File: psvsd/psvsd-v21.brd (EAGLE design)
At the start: 30 x 33.2 mm, 21 parts, among them U1 GL823(A)OG, U2 3.3V

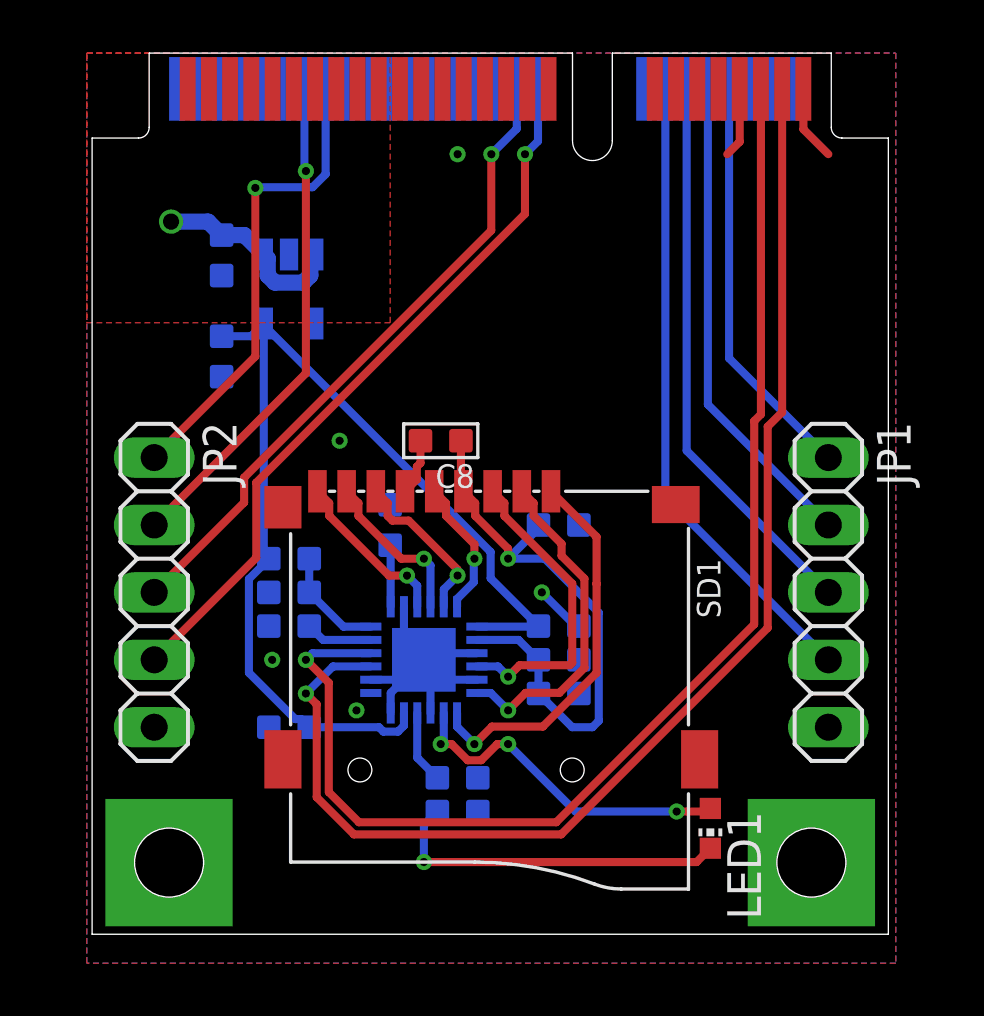
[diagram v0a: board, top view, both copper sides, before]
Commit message: Finished silkscreen and added BOM for v2.1 design
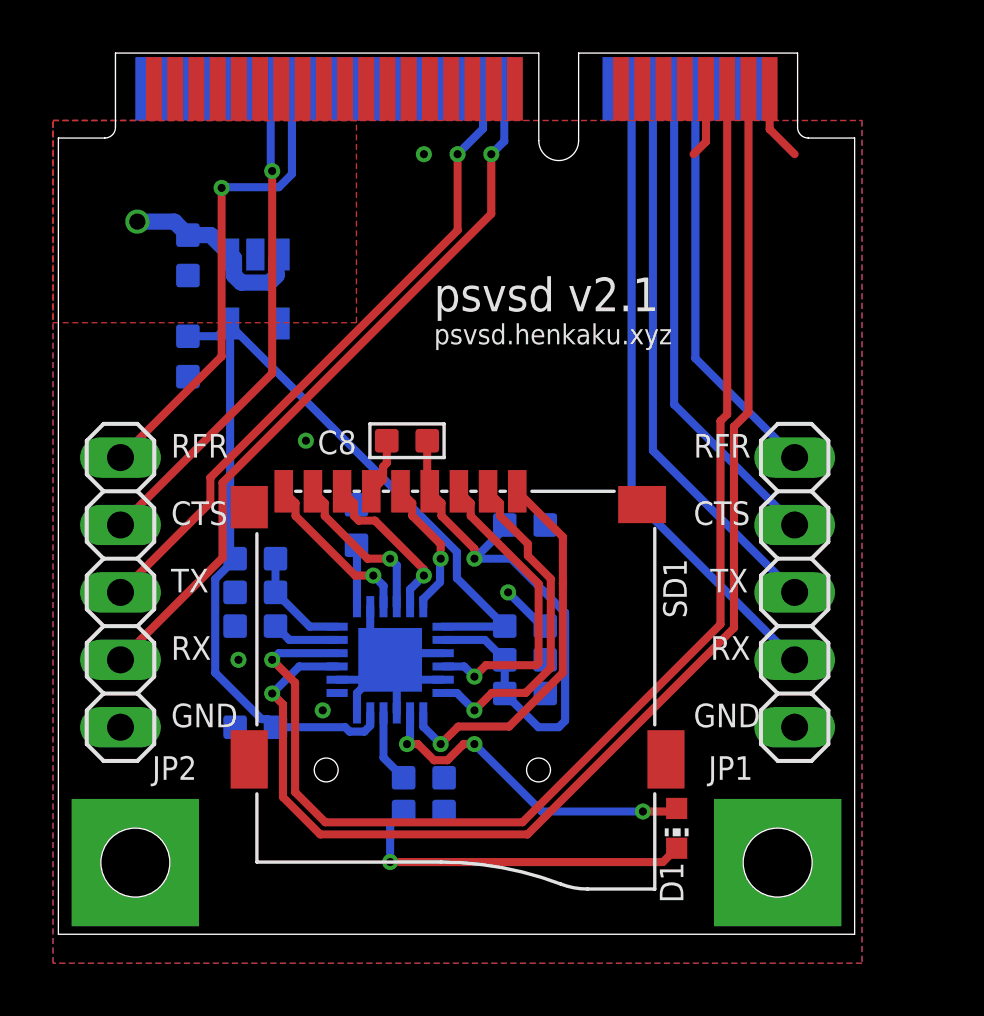
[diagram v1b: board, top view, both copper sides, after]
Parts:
- removed LED1: BLUE, led:CHIP-LED0603
- added D1: BLUE, led:CHIP-LED0603
- moved SD1 1.27 mm to (15.2, 17.8)
- moved U1 1.27 mm to (12.7, 11.4)
- moved C2 1.27 mm to (7.62, 14.0)
- moved C7 1.27 mm to (7.62, 8.89)
- moved FB1 1.27 mm to (7.62, 15.2)
- moved R1 1.27 mm to (7.62, 12.7)
- moved U2 1.27 mm to (7.62, 25.4)
- moved JP2 1.27 mm to (2.54, 14.0)
- moved C1 1.27 mm to (14.0, 6.99)
- moved C10 1.27 mm to (5.08, 26.7)
- moved C3 1.27 mm to (17.8, 11.4)
- moved C4 1.27 mm to (17.8, 16.5)
- moved C5 1.27 mm to (11.4, 16.5)
- moved C6 1.27 mm to (17.8, 12.7)
- moved C8 1.27 mm to (13.3, 19.7)
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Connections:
- net LED: now also D1.A; no longer LED1.A
- net LED_N: now also D1.C; no longer LED1.C
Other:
- outline, holes or cut-outs redrawn
- board text added: "CTS"
- board text added: "GND"
- board text added: "RFR"
- board text added: "RX"
- board text added: "TX"
- board text added: "psvsd v2.1"
- board text added: "psvsd.henkaku.xyz"

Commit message: Fixed problem where shield is not grounded
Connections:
- net GND: now also SD1.G1, SD1.G2, SD1.G3, SD1.G4
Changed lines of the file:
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@@
 <element name="C1" library="Seeed-Capacitor" library_urn="urn:adsk.eagle:library:464" package="C0603" value="0.1uF" x="13.97" y="6.985" smashed="yes" rot="MR270">
 <attribute name="MPN" value="GRM1885C1H102JA01D" x="13.97" y="6.985" size="1.778" layer="28" rot="MR270" display="off"/>
+<attribute name="NAME" x="12.7" y="7.239" size="0.635" layer="34" ratio="10" rot="MR180"/>
 <attribute name="NAME" x="17.145" y="6.604" size="0.889" layer="26" ratio="11" rot="MR0"/>
-<attribute name="NAME" x="12.7" y="7.239" size="0.635" layer="34" ratio="10" rot="MR180"/>
 <attribute name="VALUE" x="12.7" y="7.3025" size="0.635" layer="28" ratio="10" rot="MR180"/>
 </element>
 <element name="C10" library="Seeed-Capacitor" library_urn="urn:adsk.eagle:library:464" package="C0603" value="1uF" x="5.08" y="26.67" smashed="yes" rot="MR0">
 <attribute name="MPN" value="GRM1885C1H102JA01D" x="5.08" y="26.67" size="1.778" layer="28" rot="MR0" display="off"/>
+<attribute name="NAME" x="5.461" y="31.115" size="0.889" layer="26" ratio="11" rot="MR270"/>
 <attribute name="NAME" x="5.334" y="27.94" size="0.635" layer="34" ratio="10" rot="MR270"/>
-<attribute name="NAME" x="5.461" y="31.115" size="0.889" layer="26" ratio="11" rot="MR270"/>
 <attribute name="VALUE" x="5.3975" y="27.94" size="0.635" layer="28" ratio="10" rot="MR270"/>
 </element>
 <element name="C2" library="Seeed-Capacitor" library_urn="urn:adsk.eagle:library:464" package="C0603" value="0.1uF" x="7.62" y="13.97" smashed="yes" rot="MR90">
 <attribute name="MPN" value="GRM1885C1H102JA01D" x="7.62" y="13.97" size="1.778" layer="28" rot="MR90" display="off"/>
+<attribute name="NAME" x="8.89" y="13.716" size="0.635" layer="34" ratio="10" rot="MR0"/>
 <attribute name="NAME" x="5.715" y="13.589" size="0.889" layer="26" ratio="11" rot="MR0"/>
-<attribute name="NAME" x="8.89" y="13.716" size="0.635" layer="34" ratio="10" rot="MR0"/>
 <attribute name="VALUE" x="8.89" y="13.6525" size="0.635" layer="28" ratio="10" rot="MR0"/>
 </element>
 <element name="C3" library="Seeed-Capacitor" library_urn="urn:adsk.eagle:library:464" package="C0603" value="0.1uF" x="17.78" y="11.43" smashed="yes" rot="MR270">
 <attribute name="MPN" value="GRM1885C1H102JA01D" x="17.78" y="11.43" size="1.778" layer="28" rot="MR270" display="off"/>
+<attribute name="NAME" x="16.51" y="11.684" size="0.635" layer="34" ratio="10" rot="MR180"/>
 <attribute name="NAME" x="19.685" y="11.811" size="0.889" layer="26" ratio="11" rot="MR180"/>
-<attribute name="NAME" x="16.51" y="11.684" size="0.635" layer="34" ratio="10" rot="MR180"/>
 <attribute name="VALUE" x="16.51" y="11.7475" size="0.635" layer="28" ratio="10" rot="MR180"/>
 </element>
 <element name="C4" library="Seeed-Capacitor" library_urn="urn:adsk.eagle:library:464" package="C0603" value="10uF" x="17.78" y="16.51" smashed="yes" rot="MR270">
 <attribute name="MPN" value="GRM1885C1H102JA01D" x="17.78" y="16.51" size="1.778" layer="28" rot="MR270" display="off"/>
+<attribute name="NAME" x="16.51" y="16.764" size="0.635" layer="34" ratio="10" rot="MR180"/>
 <attribute name="NAME" x="19.685" y="16.891" size="0.889" layer="26" ratio="11" rot="MR180"/>
-<attribute name="NAME" x="16.51" y="16.764" size="0.635" layer="34" ratio="10" rot="MR180"/>
 <attribute name="VALUE" x="16.51" y="18.0975" size="0.635" layer="28" ratio="10" rot="MR180"/>
 </element>
 <element name="C5" library="Seeed-Capacitor" library_urn="urn:adsk.eagle:library:464" package="C0603" value="0.1uF" x="11.43" y="16.51" smashed="yes" rot="MR180">
 <attribute name="MPN" value="GRM1885C1H102JA01D" x="11.43" y="16.51" size="1.778" layer="28" rot="MR180" display="off"/>
+<attribute name="NAME" x="11.176" y="15.24" size="0.635" layer="34" ratio="10" rot="MR90"/>
 <attribute name="NAME" x="11.049" y="18.415" size="0.889" layer="26" ratio="11" rot="MR90"/>
-<attribute name="NAME" x="11.176" y="15.24" size="0.635" layer="34" ratio="10" rot="MR90"/>
 <attribute name="VALUE" x="11.1125" y="15.24" size="0.635" layer="28" ratio="10" rot="MR90"/>
 </element>
 <element name="C6" library="Seeed-Capacitor" library_urn="urn:adsk.eagle:library:464" package="C0603" value="0.1uF" x="17.78" y="12.7" smashed="yes" rot="MR270">
 <attribute name="MPN" value="GRM1885C1H102JA01D" x="17.78" y="12.7" size="1.778" layer="28" rot="MR270" display="off"/>
+<attribute name="NAME" x="16.51" y="12.954" size="0.635" layer="34" ratio="10" rot="MR180"/>
 <attribute name="NAME" x="19.685" y="13.081" size="0.889" layer="26" ratio="11" rot="MR180"/>
-<attribute name="NAME" x="16.51" y="12.954" size="0.635" layer="34" ratio="10" rot="MR180"/>
 <attribute name="VALUE" x="16.51" y="13.0175" size="0.635" layer="28" ratio="10" rot="MR180"/>
 </element>
 <element name="C7" library="Seeed-Capacitor" library_urn="urn:adsk.eagle:library:464" package="C0603" value="10uF" x="7.62" y="8.89" smashed="yes" rot="MR90">
 <attribute name="MPN" value="GRM1885C1H102JA01D" x="7.62" y="8.89" size="1.778" layer="28" rot="MR90" display="off"/>
+<attribute name="NAME" x="8.89" y="8.636" size="0.635" layer="34" ratio="10" rot="MR0"/>
 <attribute name="NAME" x="5.715" y="8.509" size="0.889" layer="26" ratio="11" rot="MR0"/>
-<attribute name="NAME" x="8.89" y="8.636" size="0.635" layer="34" ratio="10" rot="MR0"/>
 <attribute name="VALUE" x="8.89" y="8.5725" size="0.635" layer="28" ratio="10" rot="MR0"/>
 </element>
 <element name="C8" library="Seeed-Capacitor" library_urn="urn:adsk.eagle:library:464" package="C0603" value="0.1uF" x="13.335" y="19.685" smashed="yes" rot="R270">
 <attribute name="MPN" value="GRM1885C1H102JA01D" x="13.335" y="19.685" size="1.778" layer="27" rot="R270" display="off"/>
+<attribute name="NAME" x="11.43" y="20.066" size="0.889" layer="25" ratio="11" rot="R180"/>
 <attribute name="NAME" x="14.605" y="19.939" size="0.635" layer="33" ratio="10" rot="R180"/>
-<attribute name="NAME" x="11.43" y="20.066" size="0.889" layer="25" ratio="11" rot="R180"/>
 <attribute name="VALUE" x="14.605" y="21.2725" size="0.635" layer="27" ratio="10" rot="R180"/>
 </element>
 <element name="C9" library="Seeed-Capacitor" library_urn="urn:adsk.eagle:library:464" package="C0603" value="1uF" x="5.08" y="22.86" smashed="yes" rot="MR0">
 <attribute name="MPN" value="GRM1885C1H102JA01D" x="5.08" y="22.86" size="1.778" layer="28" rot="MR0" display="off"/>
+<attribute name="NAME" x="5.461" y="20.955" size="0.889" layer="26" ratio="11" rot="MR270"/>
 <attribute name="NAME" x="5.334" y="24.13" size="0.635" layer="34" ratio="10" rot="MR270"/>
-<attribute name="NAME" x="5.461" y="20.955" size="0.889" layer="26" ratio="11" rot="MR270"/>
 <attribute name="VALUE" x="5.3975" y="24.13" size="0.635" layer="28" ratio="10" rot="MR270"/>
 </element>
@@
 <wire x1="27" y1="31.42" x2="27.94" y2="30.48" width="0.3048" layer="1"/>
 <via x="13.97" y="30.48" extent="1-16" drill="0.3048"/>
+<contactref element="SD1" pad="G4"/>
+<contactref element="SD1" pad="G3"/>
+<contactref element="SD1" pad="G1"/>
+<contactref element="SD1" pad="G2"/>
 </signal>
 <signal name="VDD33">
